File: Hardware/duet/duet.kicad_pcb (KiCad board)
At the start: 2 copper layers, 2 parts, among them U1 LFE5U-45F-6BG256C, U2 W956D8MBYA5I

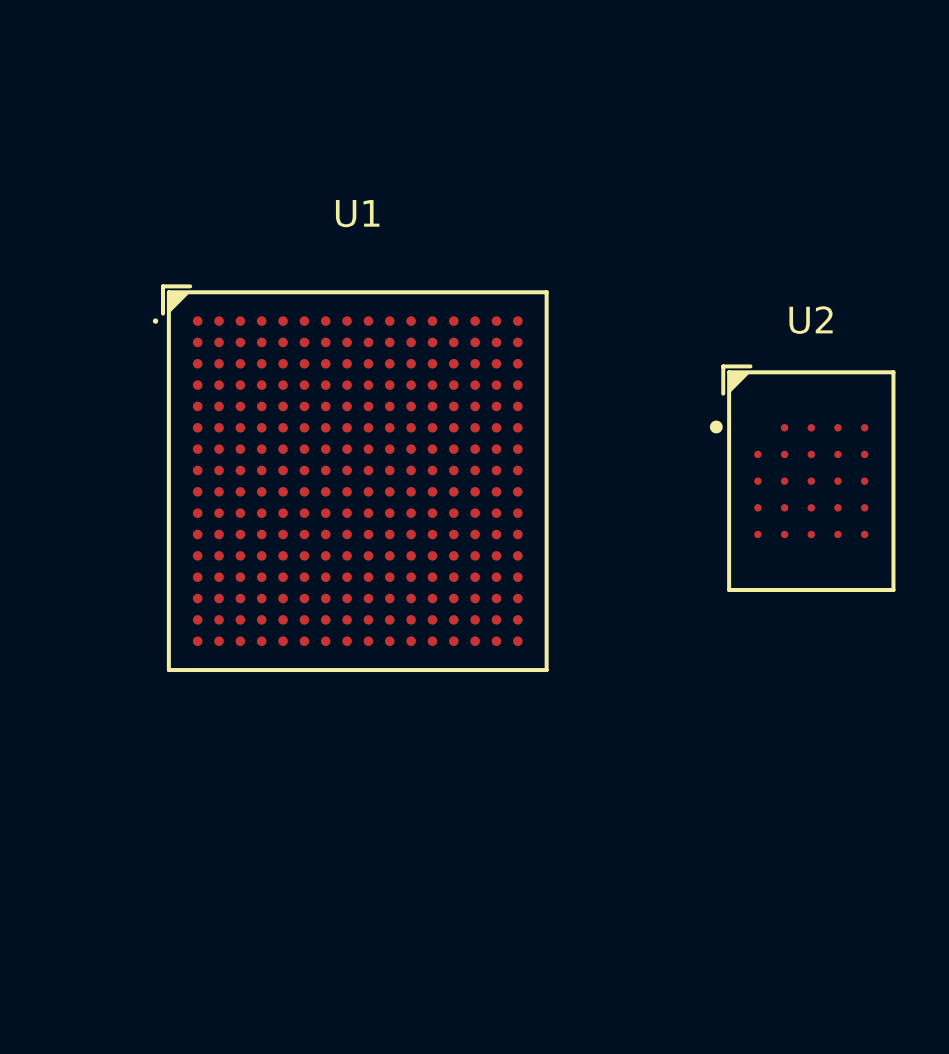
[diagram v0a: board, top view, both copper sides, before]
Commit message: Add ECP5 configuration pins and labels
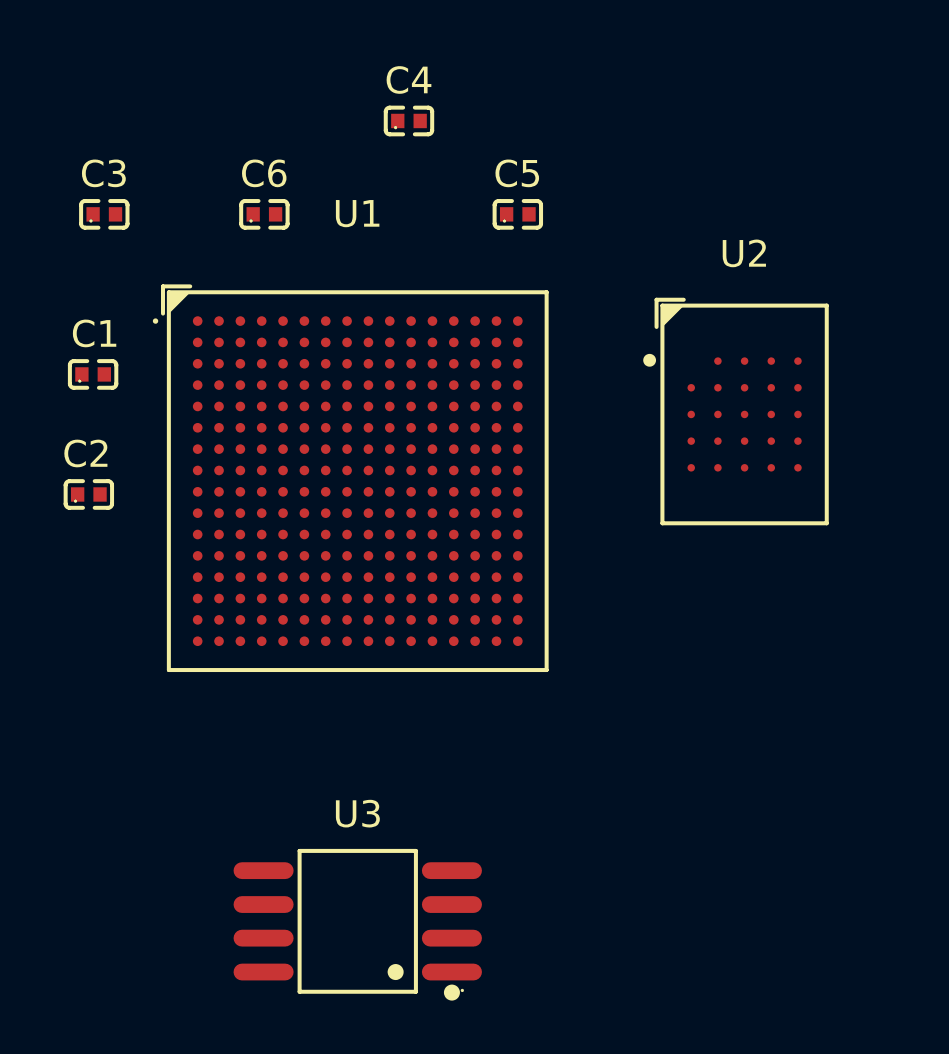
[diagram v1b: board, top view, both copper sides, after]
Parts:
- added C1: 100 nF, easyeda2kicad:C0402, F.Cu at (101.1, 76.5)
- added C2: 100 nF, easyeda2kicad:C0402, F.Cu at (100.9, 81.0)
- added C3: 100 nF, easyeda2kicad:C0402, F.Cu at (101.5, 70.5)
- added C4: 100 nF, easyeda2kicad:C0402, F.Cu at (112.9, 67.0)
- added C5: 100 nF, easyeda2kicad:C0402, F.Cu at (117.0, 70.5)
- added C6: 100 nF, easyeda2kicad:C0402, F.Cu at (107.5, 70.5)
- added U3: W25Q128JVSIQTR, easyeda2kicad:SOIC-8_L5.3-W5.3-P1.27-LS8.0-BL, F.Cu at (111.0, 97.0)
- moved U2 3.54 mm to (125.5, 78.0)
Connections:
- U1 pad A1: unconnected-(U1C-GND-PadA1) -> GND
- U1 pad A16: unconnected-(U1C-GND-PadA16) -> GND
- U1 pad B15: /FPGA Top/RAM-D1 -> RAM-DQ1
- U1 pad B16: /FPGA Top/RAM-D0 -> RAM-DQ0
- U1 pad C15: /FPGA Top/RAM-D3 -> RAM-DQ3
- U1 pad C16: /FPGA Top/RAM-D2 -> RAM-DQ2
- U1 pad D15: unconnected-(U1C-GND-PadD15) -> GND
- U1 pad D16: /FPGA Top/RAM-D4 -> RAM-DQ4
- U1 pad D2: unconnected-(U1C-GND-PadD2) -> GND
- U1 pad E15: /FPGA Top/RAM-D5 -> RAM-DQ5
- U1 pad E16: unconnected-(U1A-PR20D-PadE16) -> RAM-~{RESET}
- U1 pad F16: unconnected-(U1A-PR23A-PadF16) -> RAM-CK
- U1 pad F8: unconnected-(U1C-GND-PadF8) -> GND
- U1 pad F9: unconnected-(U1C-GND-PadF9) -> GND
- U1 pad G10: unconnected-(U1C-GND-PadG10) -> GND
- U1 pad G12: /FPGA Top/RAM-D6 -> RAM-DQ6
- U1 pad G13: /FPGA Top/RAM-D7 -> RAM-DQ7
- U1 pad G14: unconnected-(U1A-PR23C/VREF1_2-PadG14) -> RAM-~{CS}
- U1 pad G15: unconnected-(U1A-PR23B-PadG15) -> RAM-~{CK}
- U1 pad G6: unconnected-(U1C-VCC-PadG6) -> +1V1
- U1 pad G7: unconnected-(U1C-VCC-PadG7) -> +1V1
- U1 pad G8: unconnected-(U1C-GND-PadG8) -> GND
- U1 pad G9: unconnected-(U1C-VCC-PadG9) -> +1V1
- U1 pad H1: unconnected-(U1C-GND-PadH1) -> GND
- U1 pad H10: unconnected-(U1C-GND-PadH10) -> GND
- U1 pad H11: unconnected-(U1A-VCCIO2-PadH11) -> +1V8
- U1 pad H12: unconnected-(U1A-PR26A-PadH12) -> RAM-RWDS
- U1 pad H16: unconnected-(U1C-GND-PadH16) -> GND
- U1 pad H8: unconnected-(U1C-GND-PadH8) -> GND
- U1 pad H9: unconnected-(U1C-GND-PadH9) -> GND
- U1 pad J10: unconnected-(U1C-GND-PadJ10) -> GND
- U1 pad J11: unconnected-(U1A-VCCIO2-PadJ11) -> +1V8
- U1 pad J8: unconnected-(U1C-GND-PadJ8) -> GND
- U1 pad J9: unconnected-(U1C-GND-PadJ9) -> GND
- U1 pad K10: unconnected-(U1C-GND-PadK10) -> GND
- U1 pad K6: unconnected-(U1C-GND-PadK6) -> GND
- U1 pad K7: unconnected-(U1C-GND-PadK7) -> GND
- U1 pad K8: unconnected-(U1C-GND-PadK8) -> GND
- U1 pad K9: unconnected-(U1C-GND-PadK9) -> GND
- U1 pad L10: unconnected-(U1C-VCC-PadL10) -> +1V1
- U1 pad L6: unconnected-(U1B-VCCIO8-PadL6) -> +3.3V
- U1 pad L8: unconnected-(U1C-VCC-PadL8) -> +1V1
- U1 pad L9: unconnected-(U1C-VCC-PadL9) -> +1V1
- U1 pad M10: unconnected-(U1B-TDO-PadM10) -> FPGA-TDO
- U1 pad M7: unconnected-(U1B-PB9B/D2/IO2-PadM7) -> FLASH-IO2
- U1 pad N15: unconnected-(U1C-GND-PadN15) -> GND
- U1 pad N2: unconnected-(U1C-GND-PadN2) -> GND
- U1 pad N7: unconnected-(U1B-PB9A/D3/IO3-PadN7) -> FLASH-IO3
- U1 pad N8: unconnected-(U1B-PB15A/HOLDN/DI/BUSY/CSSPIN/CEN-PadN8) -> FLASH-~{CS}
- U1 pad N9: unconnected-(U1B-CCLK/MCLK/SCK-PadN9) -> FLASH-CLK
- U1 pad R11: unconnected-(U1B-TDI-PadR11) -> FPGA-TDI
- U1 pad T1: unconnected-(U1C-GND-PadT1) -> GND
- U1 pad T10: unconnected-(U1B-TCK-PadT10) -> FPGA-TCK
- U1 pad T11: unconnected-(U1B-TMS-PadT11) -> FPGA-TMS
- U1 pad T12: unconnected-(U1C-GND-PadT12) -> GND
- U1 pad T16: unconnected-(U1C-GND-PadT16) -> GND
- U1 pad T5: unconnected-(U1C-GND-PadT5) -> GND
- U1 pad T7: unconnected-(U1B-PB11A/D1/MISO/IO1-PadT7) -> FLASH-IO1
- U1 pad T8: unconnected-(U1B-PB11B/D0/MOSI/IO0-PadT8) -> FLASH-IO0
- U2 pad A3: /RAM and Flash memory/RAM-CS -> RAM-~{CS}
- U2 pad A4: /RAM and Flash memory/RAM-RESET -> RAM-~{RESET}
- U2 pad B1: /RAM and Flash memory/RAM-~{CK} -> RAM-~{CK}
- U2 pad B2: /RAM and Flash memory/RAM-CK -> RAM-CK
- U2 pad C3: unconnected-(U2-RWDS-PadC3) -> RAM-RWDS
- U2 pad C4: /RAM and Flash memory/RAM-DQ2 -> RAM-DQ2
- U2 pad D2: /RAM and Flash memory/RAM-DQ1 -> RAM-DQ1
- U2 pad D3: /RAM and Flash memory/RAM-DQ0 -> RAM-DQ0
- U2 pad D4: /RAM and Flash memory/RAM-DQ3 -> RAM-DQ3
- U2 pad D5: /RAM and Flash memory/RAM-DQ4 -> RAM-DQ4
- U2 pad E1: /RAM and Flash memory/RAM-DQ7 -> RAM-DQ7
- U2 pad E2: /RAM and Flash memory/RAM-DQ6 -> RAM-DQ6
- U2 pad E3: /RAM and Flash memory/RAM-DQ5 -> RAM-DQ5

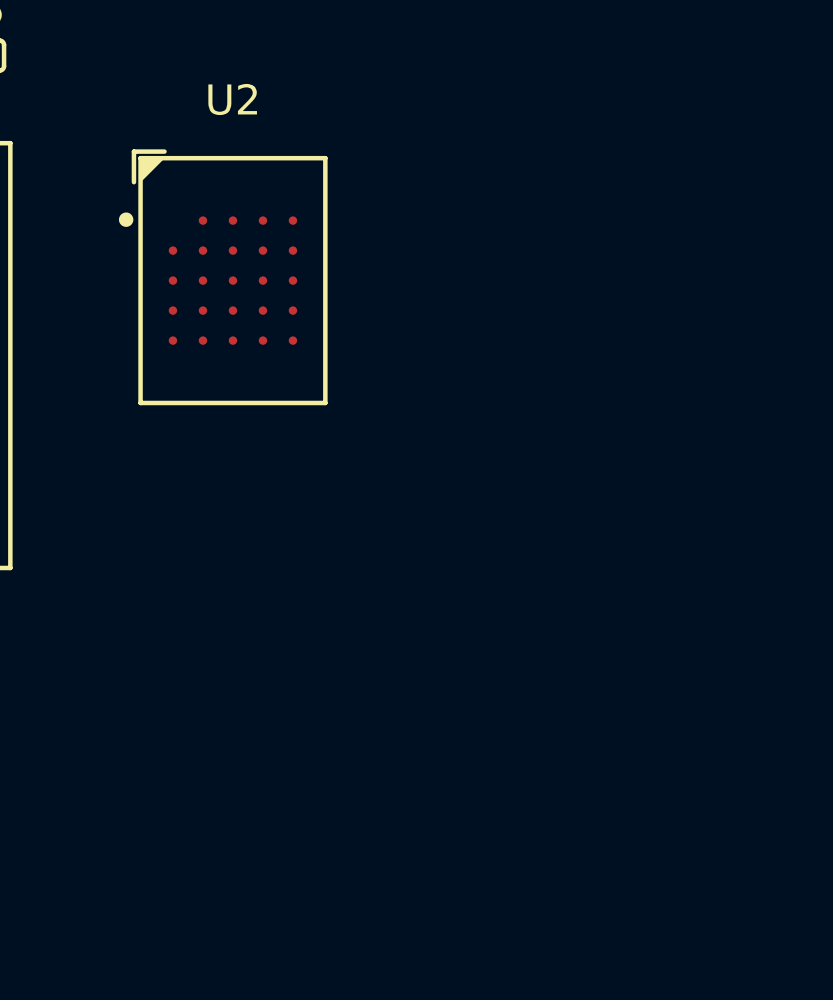
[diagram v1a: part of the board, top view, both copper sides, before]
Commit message: Adds HDMI transmitter and connector
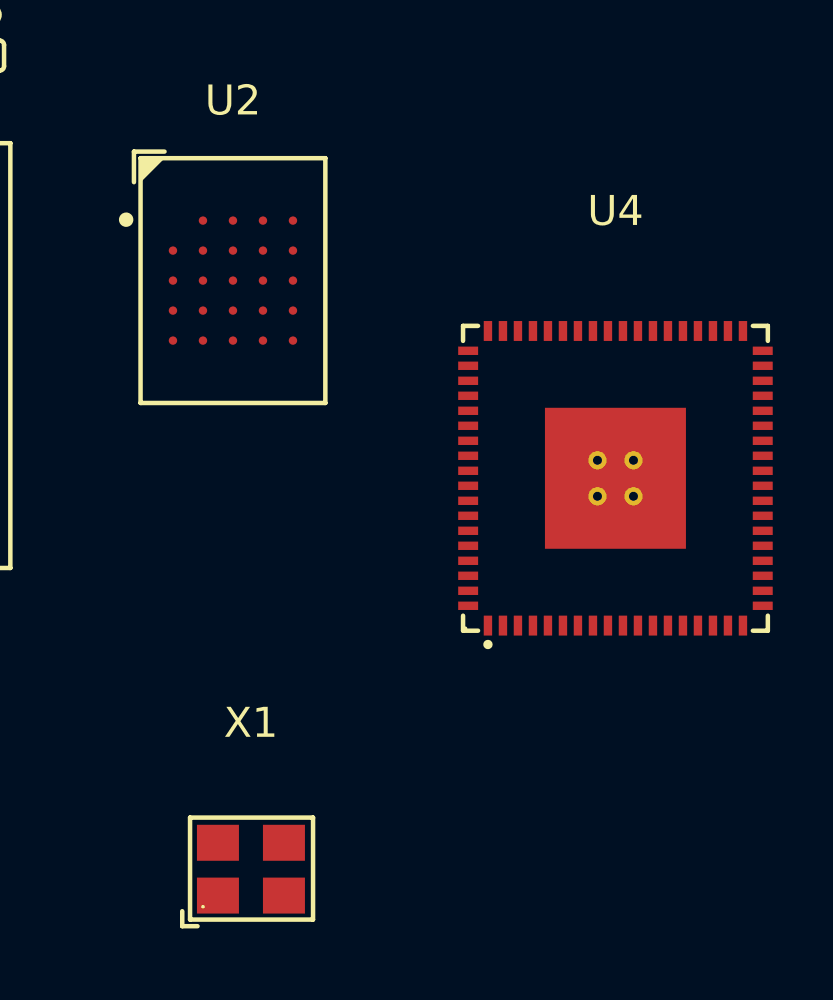
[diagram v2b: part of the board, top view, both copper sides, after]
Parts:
- added U4: SII9022ACNU, easyeda2kicad:QFN-72_L10.0-W10.0-P0.50-BL-EP, F.Cu at (138.2, 84.6)
- added X1: OT322525MJBA4SL, easyeda2kicad:OSC-SMD_4P-L3.2-W2.5-BL, F.Cu at (126.1, 97.6)
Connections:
- net RAM-CK renamed CK
- net RAM-DQ0 renamed DQ0
- net RAM-DQ1 renamed DQ1
- net RAM-DQ2 renamed DQ2
- net RAM-DQ3 renamed DQ3
- net RAM-DQ4 renamed DQ4
- net RAM-DQ5 renamed DQ5
- net RAM-DQ6 renamed DQ6
- net RAM-DQ7 renamed DQ7
- net RAM-~{CK} renamed ~{CK}
- net RAM-~{CS} renamed ~{CS}
- net RAM-~{RESET} renamed ~{RESET}
- U1 pad B8: unconnected-(U1A-PT44B/PCLKC1_0-PadB8) -> /FPGA Top/FPGA-PCLK
- U1 pad H12: RAM-RWDS -> RWDS
- U1 pad P9: unconnected-(U1B-DONE-PadP9) -> FPGA-DONE
- U1 pad R9: unconnected-(U1B-PROGRAMN-PadR9) -> FPGA-PROGRAMN
- U1 pad T9: unconnected-(U1B-INITN-PadT9) -> FPGA-INITN
- U2 pad C3: RAM-RWDS -> unconnected-(U2-RWDS-PadC3)

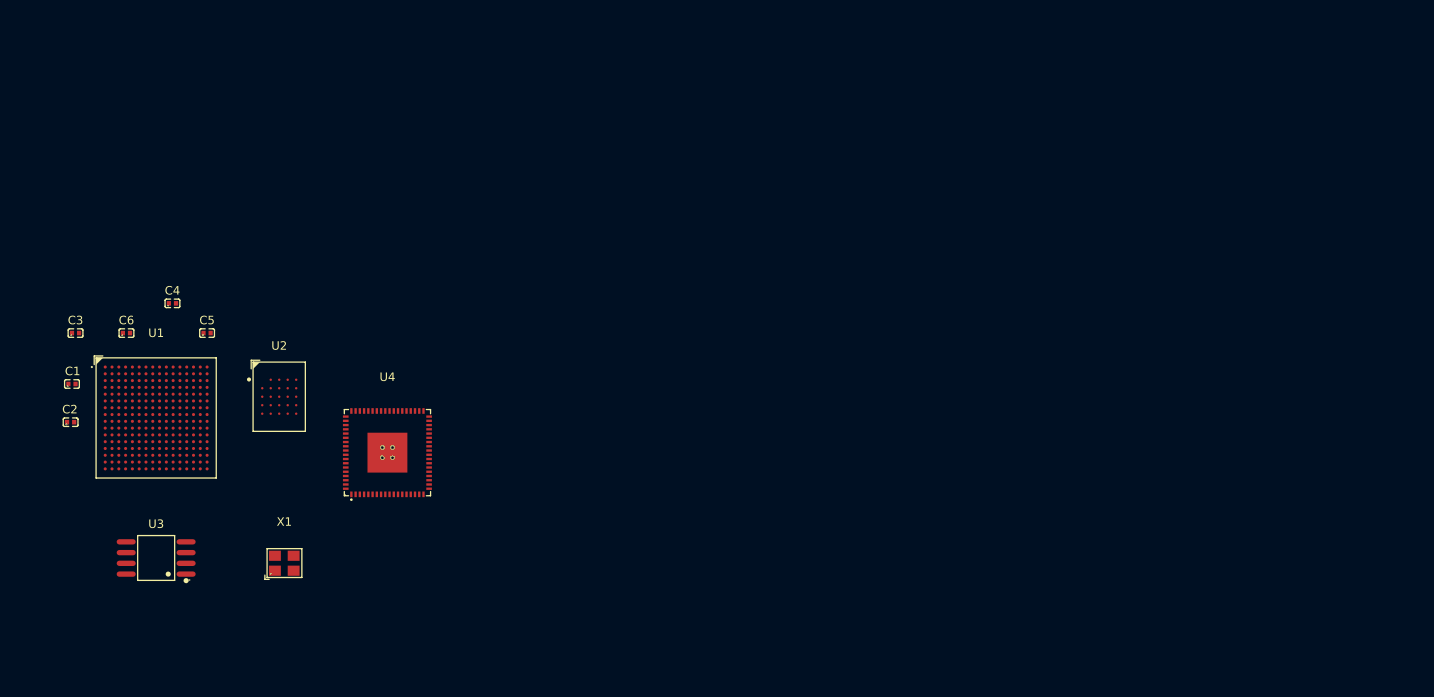
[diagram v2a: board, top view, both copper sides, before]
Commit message: Adds ESP32 and pull up-down resistors
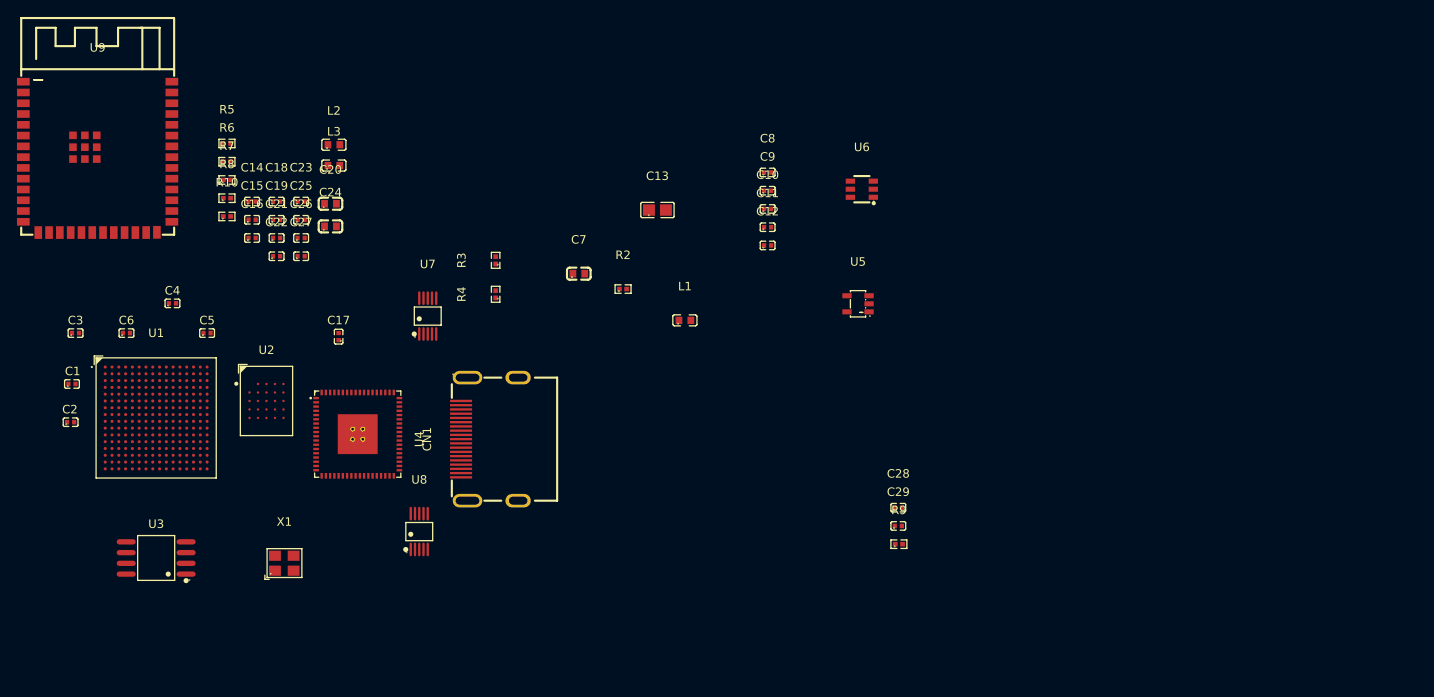
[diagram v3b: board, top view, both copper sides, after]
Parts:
- added C10: 100 nF, easyeda2kicad:C0402, F.Cu at (183.0, 55.9)
- added C11: 100 nF, easyeda2kicad:C0402, F.Cu at (183.0, 58.0)
- added C12: 10 nF, easyeda2kicad:C0402, F.Cu at (183.0, 60.2)
- added C13: 22 uF, easyeda2kicad:C0805, F.Cu at (170.1, 56.0)
- added C14: 100 nF, easyeda2kicad:C0402, F.Cu at (122.3, 55.0)
- added C15: 100 nF, easyeda2kicad:C0402, F.Cu at (122.3, 57.1)
- added C16: 100 nF, easyeda2kicad:C0402, F.Cu at (122.3, 59.3)
- added C17: 100 nF, easyeda2kicad:C0402, F.Cu at (132.5, 70.9)
- added C18: 100 nF, easyeda2kicad:C0402, F.Cu at (125.2, 55.0)
- added C19: 100 nF, easyeda2kicad:C0402, F.Cu at (125.2, 57.1)
- added C20: 10 uF, easyeda2kicad:C0603, F.Cu at (131.5, 55.3)
- added C21: 100 nF, easyeda2kicad:C0402, F.Cu at (125.2, 59.3)
- added C22: 100 nF, easyeda2kicad:C0402, F.Cu at (125.2, 61.5)
- added C23: 100 nF, easyeda2kicad:C0402, F.Cu at (128.1, 55.0)
- added C24: 10 uF, easyeda2kicad:C0603, F.Cu at (131.5, 57.9)
- added C25: 100 nF, easyeda2kicad:C0402, F.Cu at (128.1, 57.1)
- added C26: 100 nF, easyeda2kicad:C0402, F.Cu at (128.1, 59.3)
- added C27: 100 nF, easyeda2kicad:C0402, F.Cu at (128.1, 61.5)
- added C28: 100 nF, easyeda2kicad:C0402, F.Cu at (198.4, 91.1)
- added C29: CL05B104KO5NNNC, easyeda2kicad:C0402, F.Cu at (198.4, 93.2)
- added C7: 10 uF, easyeda2kicad:C0603, F.Cu at (160.8, 63.5)
- added C8: 10 nF, easyeda2kicad:C0402, F.Cu at (183.0, 51.6)
- added C9: 100 nF, easyeda2kicad:C0402, F.Cu at (183.0, 53.7)
- added CN1: A71-05H5-111N1, easyeda2kicad:HDMI-SMD_A71-05H5-111N1, F.Cu at (150.3, 83.0)
- added L1: 600ohm@100MHz, easyeda2kicad:L0603, F.Cu at (173.3, 69.0)
- added L2: 600ohm@100MHz, easyeda2kicad:L0603, F.Cu at (131.9, 48.3)
- added L3: 600ohm@100MHz, easyeda2kicad:L0603, F.Cu at (131.9, 50.8)
- added R10: 4.7k, easyeda2kicad:R0402, F.Cu at (119.3, 56.8)
- added R2: 10k, easyeda2kicad:R0402, F.Cu at (166.0, 65.3)
- added R3: 2.2k, easyeda2kicad:R0402, F.Cu at (151.0, 61.9)
- added R4: 2.2k, easyeda2kicad:R0402, F.Cu at (151.0, 65.9)
- added R5: 4.7k, easyeda2kicad:R0402, F.Cu at (119.3, 48.2)
- added R6: 4.7k, easyeda2kicad:R0402, F.Cu at (119.3, 50.3)
- added R7: 100 Ohm, easyeda2kicad:R0402, F.Cu at (119.3, 52.5)
- added R8: 4.3k, easyeda2kicad:R0402, F.Cu at (119.3, 54.6)
- added R9: 10k, easyeda2kicad:R0402, F.Cu at (198.5, 95.4)
- added U5: RT9013-12GB, easyeda2kicad:SOT-23-5_L3.0-W1.7-P0.95-LS2.8-BR, F.Cu at (193.7, 67.0)
- added U6: TPS563201DDCR, easyeda2kicad:SOT-23-6_L2.9-W1.6-P0.95-LS2.8-BR, F.Cu at (194.2, 53.5)
- added U7: RCLAMP0514M, easyeda2kicad:MSOP-10_L3.0-W3.0-P0.50-LS5.0-BL, F.Cu at (143.0, 68.5)
- added U8: RCLAMP0514M, easyeda2kicad:MSOP-10_L3.0-W3.0-P0.50-LS5.0-BL, F.Cu at (142.0, 93.9)
- added U9: ESP32-S3-WROOM-1, easyeda2kicad:WIRELM-SMD_ESP32-S3-WROOM-1, F.Cu at (104.1, 49.8)
- moved U4 4.12 mm to (134.8, 82.4), turned to -90 degrees
- moved U2 1.58 mm to (124.0, 78.5)
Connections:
- net /FPGA Top/FPGA-PCLK renamed /FPGA/FPGA-PCLK
- net /HDMI transmitter/HDMI-IN-D10 renamed D10
- net /HDMI transmitter/HDMI-IN-D11 renamed D11
- net /HDMI transmitter/HDMI-IN-D12 renamed D12
- net /HDMI transmitter/HDMI-IN-D13 renamed D13
- net /HDMI transmitter/HDMI-IN-D14 renamed D14
- net /HDMI transmitter/HDMI-IN-D15 renamed D15
- net /HDMI transmitter/HDMI-IN-D16 renamed D16
- net /HDMI transmitter/HDMI-IN-D17 renamed D17
- net /HDMI transmitter/HDMI-IN-D18 renamed D18
- net /HDMI transmitter/HDMI-IN-D19 renamed D19
- net /HDMI transmitter/HDMI-IN-D20 renamed D20
- net /HDMI transmitter/HDMI-IN-D21 renamed D21
- net /HDMI transmitter/HDMI-IN-D22 renamed D22
- net /HDMI transmitter/HDMI-IN-D23 renamed D23
- net /HDMI transmitter/HDMI-IN-D9 renamed D9
- U4 pad 1: unconnected-(U4-CSCL-Pad1) -> CSCL
- U4 pad 12: unconnected-(U4-CVCC12-Pad12) -> /HDMI/+1V2_CVCC
- U4 pad 2: unconnected-(U4-CSDA-Pad2) -> CSDA
- U4 pad 21: unconnected-(U4-IOVCC-Pad21) -> /HDMI/+3.3V_IOVCC
- U4 pad 22: unconnected-(U4-IDCK-Pad22) -> IDCK
- U4 pad 23: unconnected-(U4-D8-Pad23) -> D8
- U4 pad 24: unconnected-(U4-D7-Pad24) -> D7
- U4 pad 25: unconnected-(U4-D6-Pad25) -> D6
- U4 pad 26: unconnected-(U4-CVCC12-Pad26) -> /HDMI/+1V2_CVCC
- U4 pad 27: unconnected-(U4-D5-Pad27) -> D5
- U4 pad 28: unconnected-(U4-D4-Pad28) -> D4
- U4 pad 29: unconnected-(U4-D3-Pad29) -> D3
- U4 pad 3: unconnected-(U4-IOVCC-Pad3) -> /HDMI/+3.3V_IOVCC
- U4 pad 30: unconnected-(U4-D2-Pad30) -> D2
- U4 pad 31: unconnected-(U4-D1-Pad31) -> D1
- U4 pad 32: unconnected-(U4-D0-Pad32) -> D0
- U4 pad 33: unconnected-(U4-DE-Pad33) -> DE
- U4 pad 34: unconnected-(U4-HSYNC-Pad34) -> HSYNC
- U4 pad 35: unconnected-(U4-VSYNC-Pad35) -> VSYNC
- U4 pad 36: unconnected-(U4-SPDIF-Pad36) -> SPDIF
- U4 pad 42: unconnected-(U4-CVCC12-Pad42) -> /HDMI/+1V2_CVCC
- U4 pad 43: unconnected-(U4-CGND-Pad43) -> GND
- U4 pad 46: unconnected-(U4-IOVCC-Pad46) -> /HDMI/+3.3V_IOVCC
- U4 pad 47: unconnected-(U4-CVCC12-Pad47) -> /HDMI/+1V2_CVCC
- U4 pad 48: unconnected-(U4-DSDA-Pad48) -> /HDMI/DSDA
- U4 pad 49: unconnected-(U4-DSCL-Pad49) -> /HDMI/DSCL
- U4 pad 5: unconnected-(U4-CVCC12-Pad5) -> /HDMI/+1V2_CVCC
- U4 pad 50: unconnected-(U4-CEC_D-Pad50) -> HDMI-CEC-D
- U4 pad 51: unconnected-(U4-~{RESET}-Pad51) -> HDMI-RESET
- U4 pad 52: unconnected-(U4-INT-Pad52) -> HDMI-INT
- U4 pad 53: unconnected-(U4-CVCC12-Pad53) -> /HDMI/+1V2_CVCC
- U4 pad 54: unconnected-(U4-HPD-Pad54) -> /HDMI/HPD
- U4 pad 55: unconnected-(U4-RSVDL-Pad55) -> GND
- U4 pad 56: unconnected-(U4-EXT_SWING-Pad56) -> /HDMI/EXT_SWING
- U4 pad 57: unconnected-(U4-IOGND-Pad57) -> GND
- U4 pad 58: unconnected-(U4-TXC--Pad58) -> /HDMI/TXC-
- U4 pad 59: unconnected-(U4-TXC+-Pad59) -> /HDMI/TXC+
- U4 pad 60: unconnected-(U4-AVCC12-Pad60) -> /HDMI/+1V2_AVCC
- U4 pad 61: unconnected-(U4-TX0--Pad61) -> /HDMI/TX0-
- U4 pad 62: unconnected-(U4-TX0+-Pad62) -> /HDMI/TX0+
- U4 pad 63: unconnected-(U4-AGND-Pad63) -> GND
- U4 pad 64: unconnected-(U4-TX1--Pad64) -> /HDMI/TX1-
- U4 pad 65: unconnected-(U4-TX1+-Pad65) -> /HDMI/TX1+
- U4 pad 66: unconnected-(U4-AVCC12-Pad66) -> /HDMI/+1V2_AVCC
- U4 pad 67: unconnected-(U4-TX2--Pad67) -> /HDMI/TX2-
- U4 pad 68: unconnected-(U4-TX2+-Pad68) -> /HDMI/TX2+
- U4 pad 69: unconnected-(U4-IO_SEL-Pad69) -> GND
- U4 pad 70: unconnected-(U4-VDDQ-Pad70) -> GND
- U4 pad 71: unconnected-(U4-CEC_A-Pad71) -> /HDMI/CEC_A
- U4 pad 72: unconnected-(U4-CI2CA-Pad72) -> CI2CA
- U4 pad 73: unconnected-(U4-EP-Pad73) -> GND
